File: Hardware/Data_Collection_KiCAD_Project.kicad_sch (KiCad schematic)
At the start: 3 parts

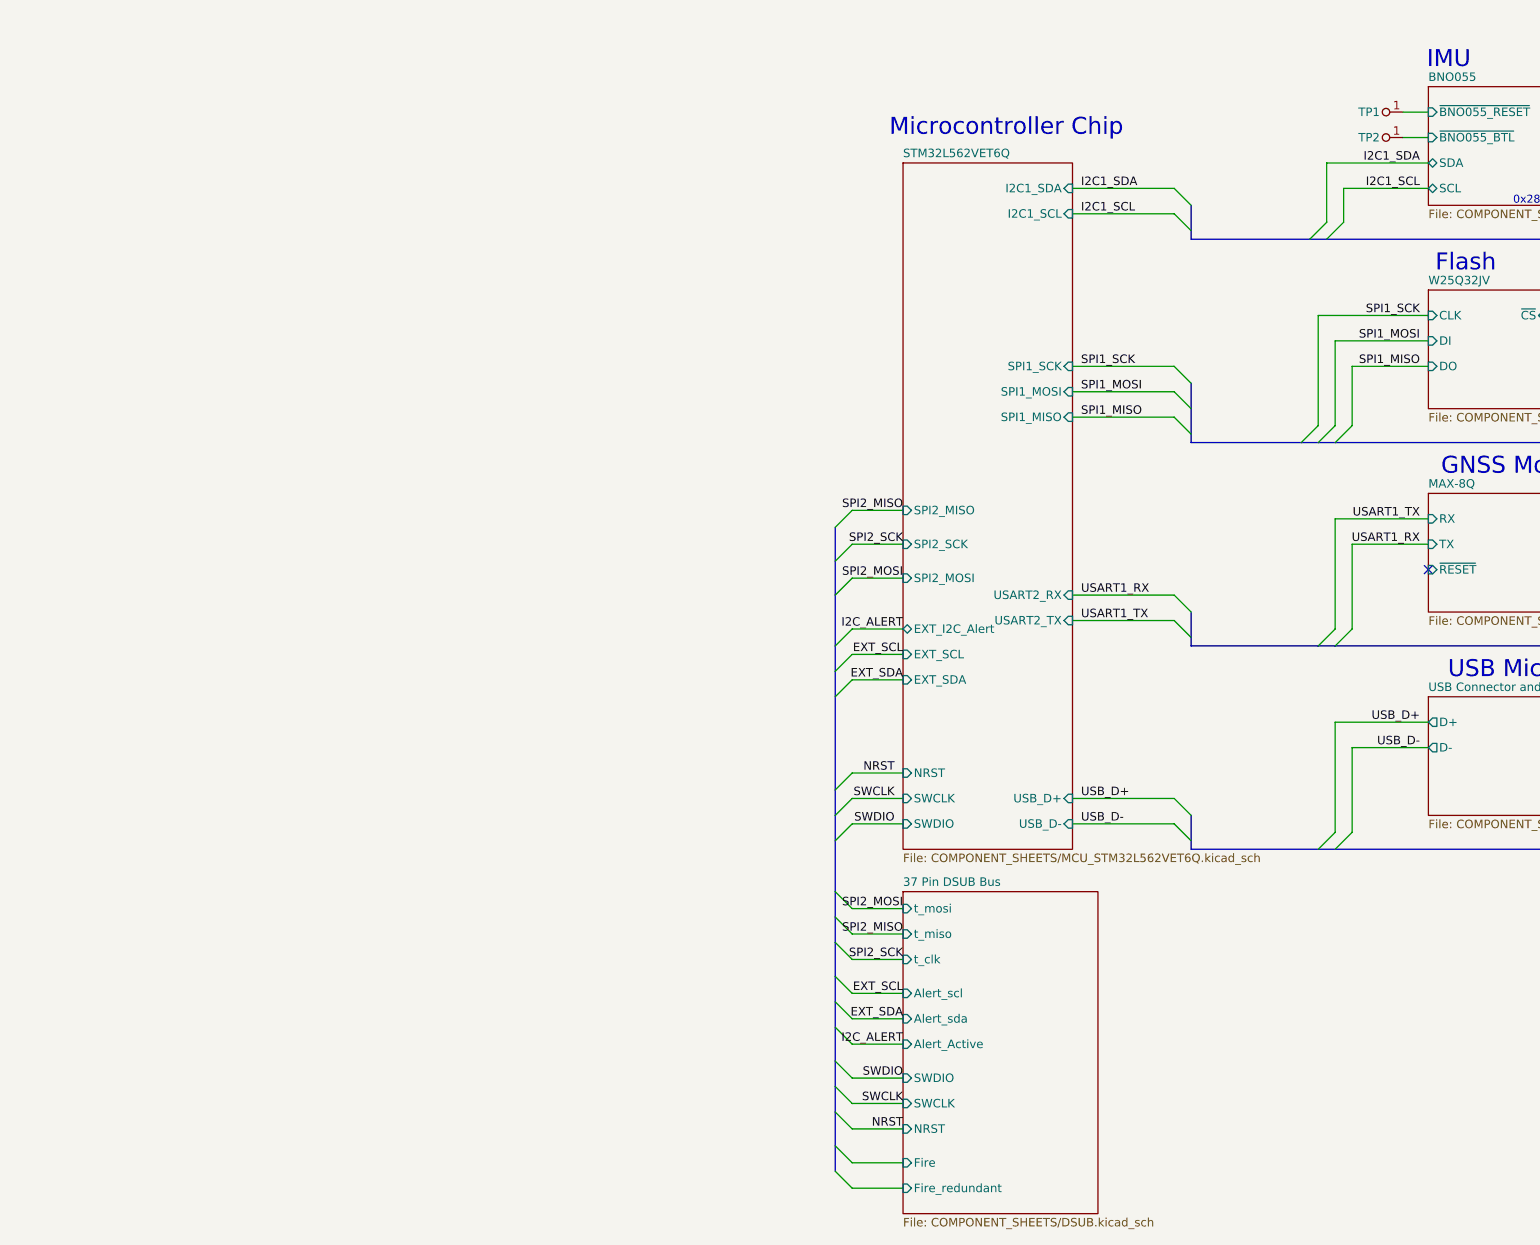
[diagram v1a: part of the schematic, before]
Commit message: Updated MCU Component Sheet
Used the file from the Telemetry board for compatibility and commonality.
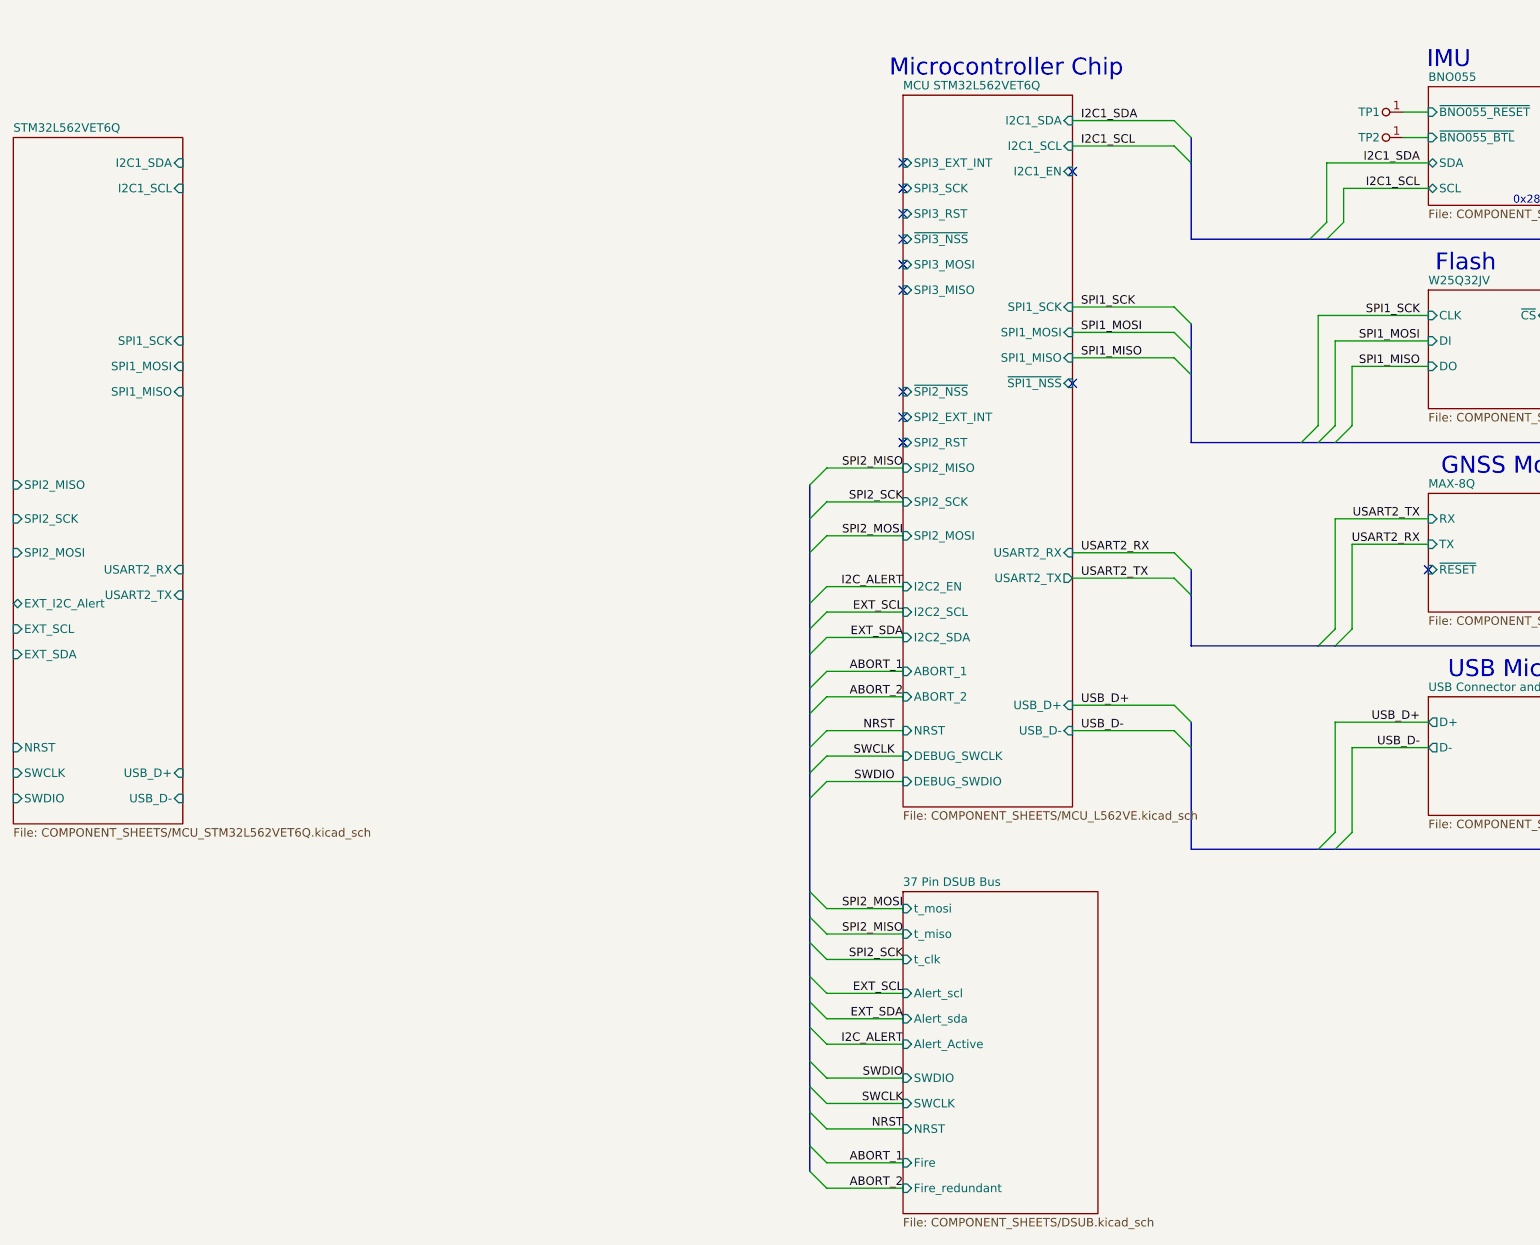
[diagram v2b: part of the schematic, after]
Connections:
- no-connect marks 3 -> 14
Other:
- added sheet MCU STM32L562VET6Q (COMPONENT_SHEETS/MCU_L562VE.kicad_sch)

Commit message: Corrected PCB edge cuts, removed components
Will be mimicking layout done by Seth Sievers
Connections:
- no-connect marks 14 -> 13
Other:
- removed sheet STM32L562VET6Q
- sheet KX134-1211 ports: added ADDR; removed none
- sheet MCU STM32L562VET6Q ports: added ~{USART2_RST}; removed none
